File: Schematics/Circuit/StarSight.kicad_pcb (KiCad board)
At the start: 2 copper layers, 21 parts, among them J10 IR1, J11 IR1, J12 ultSound1, J13 ultSound1, J14 ultSound1, J15 ultSound1, J2 Line1, J3 Line2, J4 Line3, J5 Line4, J6 Line5, J7 IR1, J8 IR1, J9 IR1, P1 CONN_13X2, P2 Power, U1 LM1084IT-5.0/NOPB

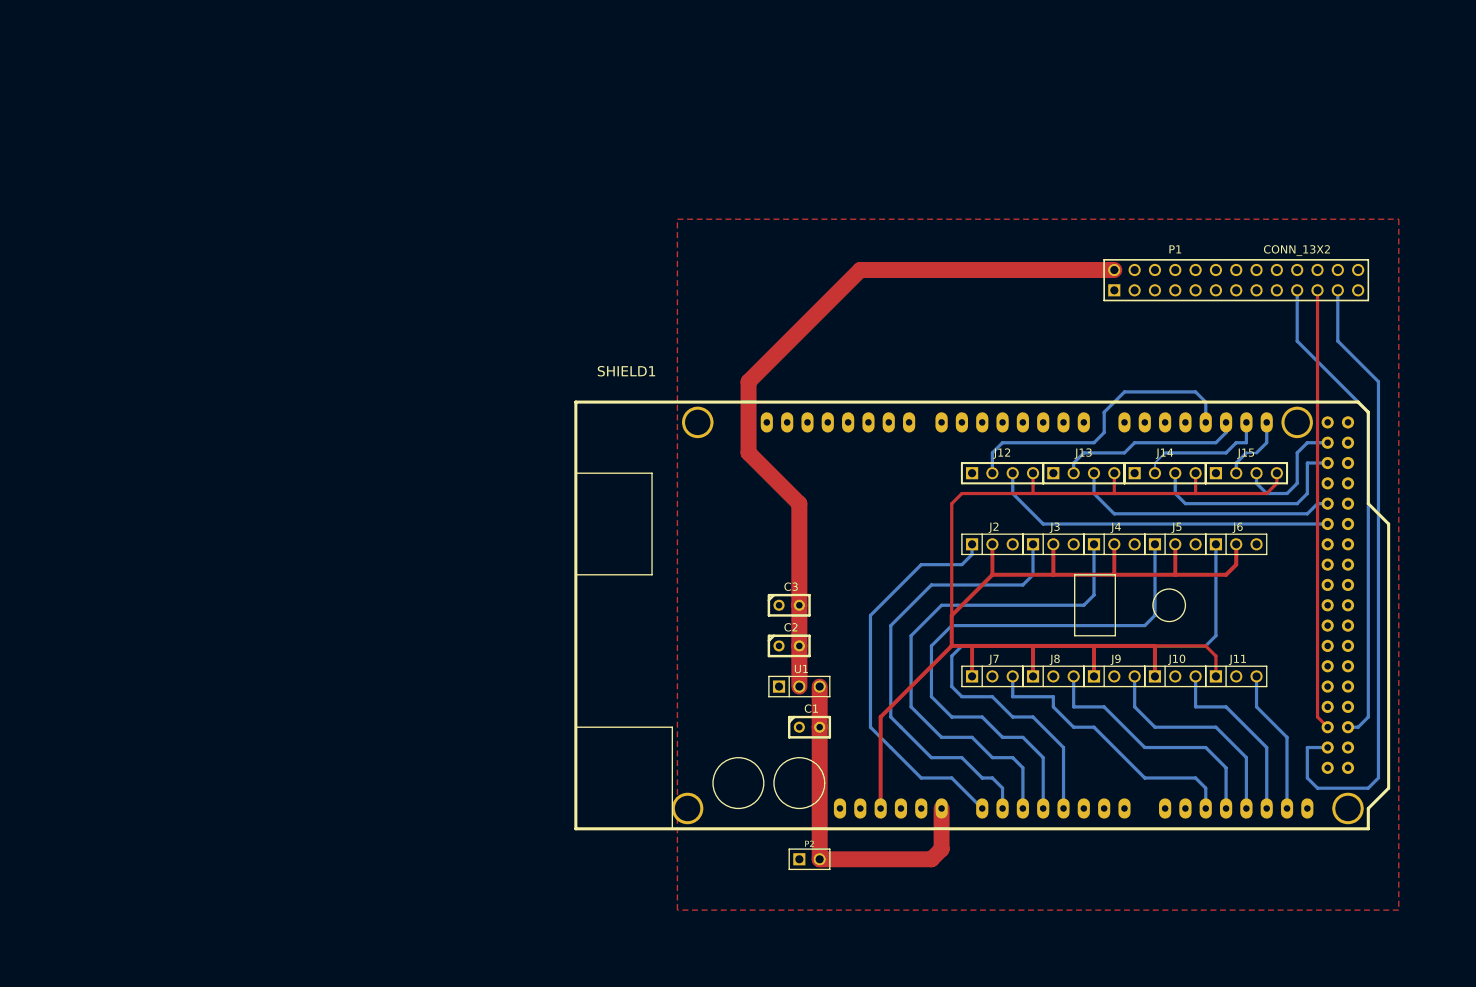
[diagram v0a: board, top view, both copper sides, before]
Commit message: Add switched regulator and motors
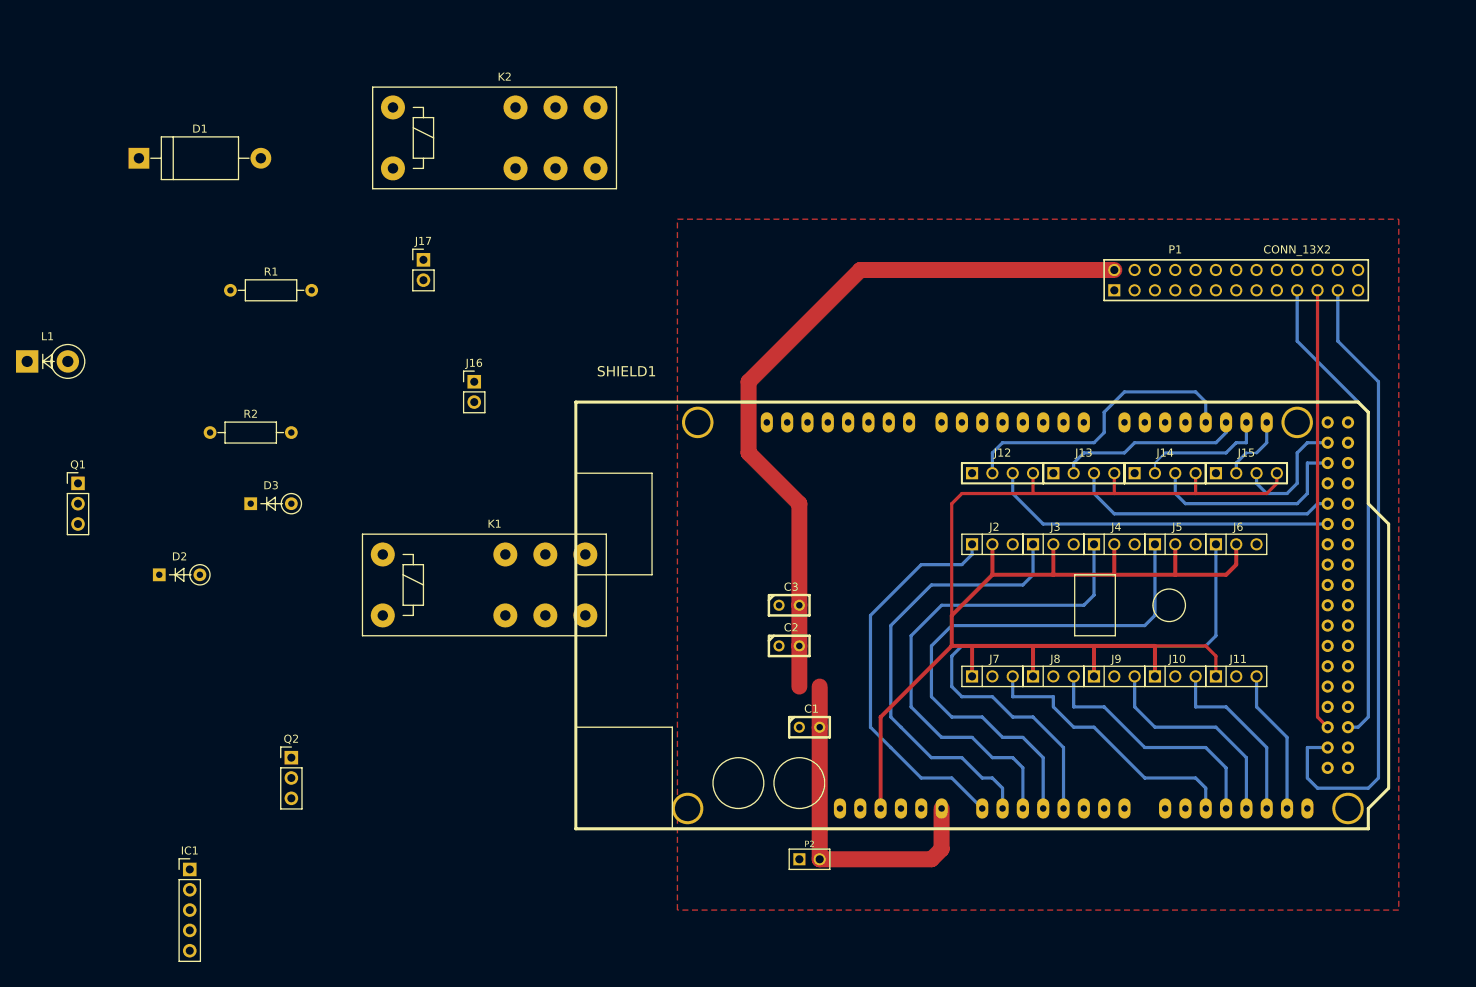
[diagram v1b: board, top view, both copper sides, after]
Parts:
- removed U1: LM1084IT-5.0/NOPB, PIN_ARRAY_3X1
- added D1: 1n5824, Diodes_THT:D_DO-201_P15.24mm_Horizontal, F.Cu at (48.3, 34.3)
- added D2: D, Diodes_THT:D_DO-35_SOD27_P5.08mm_Vertical_KathodeUp, F.Cu at (50.8, 86.4)
- added D3: D, Diodes_THT:D_DO-35_SOD27_P5.08mm_Vertical_KathodeUp, F.Cu at (62.2, 77.5)
- added IC1: LM2956-5V, Pin_Headers:Pin_Header_Straight_1x05_Pitch2.54mm, F.Cu at (54.6, 123.2)
- added J16: Conn_01x02, Pin_Headers:Pin_Header_Straight_1x02_Pitch2.54mm, F.Cu at (90.2, 62.2)
- added J17: Conn_01x02, Pin_Headers:Pin_Header_Straight_1x02_Pitch2.54mm, F.Cu at (83.8, 47.0)
- added K1: M1BS5V2-05T, Relays_THT:Relay_DPDT_Finder_40.52, F.Cu at (78.7, 83.8)
- added K2: M1BS5V2-05T, Relays_THT:Relay_DPDT_Finder_40.52, F.Cu at (80.0, 27.9)
- added L1: 33 uH, Diodes_THT:D_5W_P5.08mm_Vertical_KathodeUp, F.Cu at (34.3, 59.7)
- added Q1: Q_NMOS_GDS, Pin_Headers:Pin_Header_Straight_1x03_Pitch2.54mm, F.Cu at (40.6, 74.9)
- added Q2: Q_NMOS_GDS, Pin_Headers:Pin_Header_Straight_1x03_Pitch2.54mm, F.Cu at (67.3, 109.2)
- added R1: 10k, Resistors_THT:R_Axial_DIN0207_L6.3mm_D2.5mm_P10.16mm_Horizontal, F.Cu at (59.7, 50.8)
- added R2: 10k, Resistors_THT:R_Axial_DIN0207_L6.3mm_D2.5mm_P10.16mm_Horizontal, F.Cu at (57.1, 68.6)
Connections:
- net N-0000085 renamed +12V
- P1 pad 1: (no net) -> Net-(P1-Pad1)
- P1 pad 10: (no net) -> /RXD
- P1 pad 11: (no net) -> /GPIO22
- P1 pad 12: (no net) -> /GPIO18
- P1 pad 13: (no net) -> Net-(P1-Pad13)
- P1 pad 14: (no net) -> Net-(P1-Pad14)
- P1 pad 15: (no net) -> Net-(P1-Pad15)
- P1 pad 16: (no net) -> /GPIO23
- P1 pad 17: (no net) -> Net-(P1-Pad17)
- P1 pad 18: (no net) -> /GPIO24
- P1 pad 20: (no net) -> Net-(P1-Pad20)
- P1 pad 22: (no net) -> /GPIO25
- P1 pad 24: (no net) -> /GPIO8(CE0)
- P1 pad 25: (no net) -> Net-(P1-Pad25)
- P1 pad 26: (no net) -> /GPIO7(CE1)
- P1 pad 3: (no net) -> /GPIO0(SDA)
- P1 pad 4: (no net) -> Net-(P1-Pad4)
- P1 pad 5: (no net) -> /GPIO1(SCL)
- P1 pad 7: (no net) -> /GPIO17
- P1 pad 8: (no net) -> /TXD
- P1 pad 9: (no net) -> Net-(P1-Pad9)
- SHIELD1 pad 0: (no net) -> Net-(SHIELD1-Pad0)
- SHIELD1 pad 1: (no net) -> Net-(SHIELD1-Pad1)
- SHIELD1 pad 10: (no net) -> Net-(Q2-Pad1)
- SHIELD1 pad 11: (no net) -> Net-(K2-PadA2)
- SHIELD1 pad 12: (no net) -> Net-(Q1-Pad1)
- SHIELD1 pad 13: (no net) -> Net-(K1-PadA2)
- SHIELD1 pad 14: (no net) -> Net-(SHIELD1-Pad14)
- SHIELD1 pad 15: (no net) -> Net-(SHIELD1-Pad15)
- SHIELD1 pad 16: (no net) -> Net-(SHIELD1-Pad16)
- SHIELD1 pad 17: (no net) -> Net-(SHIELD1-Pad17)
- SHIELD1 pad 2: (no net) -> Net-(SHIELD1-Pad2)
- SHIELD1 pad 23: (no net) -> Net-(SHIELD1-Pad23)
- SHIELD1 pad 25: (no net) -> Net-(SHIELD1-Pad25)
- SHIELD1 pad 26: (no net) -> Net-(SHIELD1-Pad26)
- SHIELD1 pad 27: (no net) -> Net-(SHIELD1-Pad27)
- SHIELD1 pad 29: (no net) -> Net-(SHIELD1-Pad29)
- SHIELD1 pad 3: (no net) -> Net-(SHIELD1-Pad3)
- SHIELD1 pad 31: (no net) -> Net-(SHIELD1-Pad31)
- SHIELD1 pad 32: (no net) -> Net-(SHIELD1-Pad32)
- SHIELD1 pad 33: (no net) -> Net-(SHIELD1-Pad33)
- SHIELD1 pad 34: (no net) -> Net-(SHIELD1-Pad34)
- SHIELD1 pad 35: (no net) -> Net-(SHIELD1-Pad35)
- SHIELD1 pad 36: (no net) -> Net-(SHIELD1-Pad36)
- SHIELD1 pad 37: (no net) -> Net-(SHIELD1-Pad37)
- SHIELD1 pad 38: (no net) -> Net-(SHIELD1-Pad38)
- SHIELD1 pad 39: (no net) -> Net-(SHIELD1-Pad39)
- SHIELD1 pad 3V3: (no net) -> Net-(SHIELD1-Pad3V3)
- SHIELD1 pad 4: (no net) -> Net-(SHIELD1-Pad4)
- SHIELD1 pad 40: (no net) -> Net-(SHIELD1-Pad40)
- SHIELD1 pad 41: (no net) -> Net-(SHIELD1-Pad41)
- SHIELD1 pad 42: (no net) -> Net-(SHIELD1-Pad42)
- SHIELD1 pad 43: (no net) -> Net-(SHIELD1-Pad43)
- SHIELD1 pad 44: (no net) -> Net-(SHIELD1-Pad44)
- SHIELD1 pad 45: (no net) -> Net-(SHIELD1-Pad45)
- SHIELD1 pad 46: (no net) -> Net-(SHIELD1-Pad46)
- SHIELD1 pad 47: (no net) -> Net-(SHIELD1-Pad47)
- SHIELD1 pad 48: (no net) -> Net-(SHIELD1-Pad48)
- SHIELD1 pad 49: (no net) -> Net-(SHIELD1-Pad49)
- SHIELD1 pad 5: (no net) -> Net-(SHIELD1-Pad5)
- SHIELD1 pad 53: (no net) -> Net-(SHIELD1-Pad53)
- SHIELD1 pad 5V_4: (no net) -> Net-(SHIELD1-Pad5V_4)
- SHIELD1 pad 5V_5: (no net) -> Net-(SHIELD1-Pad5V_5)
- SHIELD1 pad 6: (no net) -> Net-(SHIELD1-Pad6)
- SHIELD1 pad 7: (no net) -> Net-(SHIELD1-Pad7)
- SHIELD1 pad 8: (no net) -> Net-(SHIELD1-Pad8)
- SHIELD1 pad 9: (no net) -> Net-(SHIELD1-Pad9)
- SHIELD1 pad AD15: (no net) -> Net-(SHIELD1-PadAD15)
- SHIELD1 pad AD5: (no net) -> Net-(SHIELD1-PadAD5)
- SHIELD1 pad AD6: (no net) -> Net-(SHIELD1-PadAD6)
- SHIELD1 pad AD7: (no net) -> Net-(SHIELD1-PadAD7)
- SHIELD1 pad AD8: (no net) -> Net-(SHIELD1-PadAD8)
- SHIELD1 pad AD9: (no net) -> Net-(SHIELD1-PadAD9)
- SHIELD1 pad AREF: (no net) -> Net-(SHIELD1-PadAREF)
- SHIELD1 pad GND1: (no net) -> Net-(SHIELD1-PadGND1)
- SHIELD1 pad GND3: (no net) -> Net-(SHIELD1-PadGND3)
- SHIELD1 pad GND4: (no net) -> Net-(SHIELD1-PadGND4)
- SHIELD1 pad GND5: (no net) -> Net-(SHIELD1-PadGND5)
- SHIELD1 pad RST: (no net) -> Net-(SHIELD1-PadRST)

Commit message: Fix pcb power suply and motors
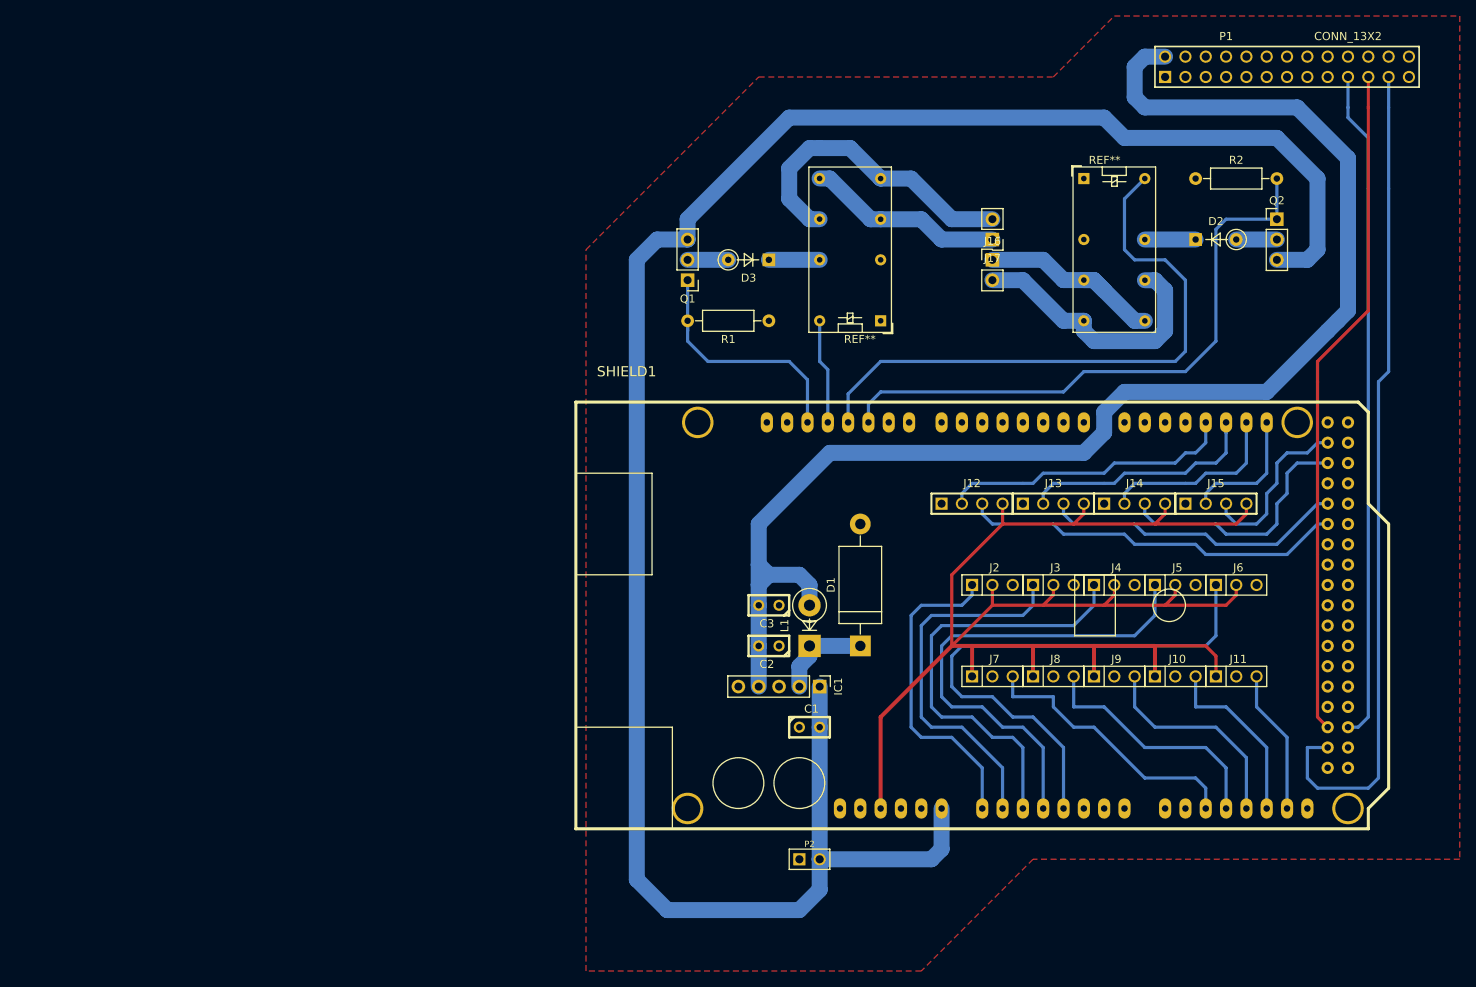
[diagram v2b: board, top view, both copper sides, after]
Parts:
- removed K1, K2: M1BS5V2-05T, Relays_THT:Relay_DPDT_Finder_40.52
- added REF**: Relay_DPDT_Omron_G5V-2, Relays_THT:Relay_DPDT_Omron_G5V-2, F.Cu at (141.0, 54.6)
- added REF**: Relay_DPDT_Omron_G5V-2, Relays_THT:Relay_DPDT_Omron_G5V-2, F.Cu at (166.4, 36.8)
- moved Q2 140.4 mm to (190.5, 41.9)
- moved D2 136.2 mm to (180.3, 44.5)
- moved R2 127.2 mm to (180.3, 36.8)
- moved D1 108.8 mm to (138.4, 95.2), turned to 90 degrees
- moved L1 104.1 mm to (132.1, 95.2), turned to 90 degrees
- moved IC1 82.0 mm to (133.3, 100.3), turned to 270 degrees
- moved Q1 80.3 mm to (116.8, 49.5), turned to 180 degrees
- moved D3 71.6 mm to (127.0, 47.0), turned to 180 degrees
- moved J17 71.2 mm to (154.9, 44.5), turned to 180 degrees
- moved R1 67.4 mm to (127.0, 54.6), turned to 180 degrees
- moved J16 66.5 mm to (154.9, 47.0)
- moved P1 27.4 mm to (191.8, 22.9)
- moved J12 5.39 mm to (152.4, 77.5)
- moved J13 5.39 mm to (162.6, 77.5)
- moved J14 5.39 mm to (172.7, 77.5)
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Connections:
- SHIELD1 pad 12: Net-(Q1-Pad1) -> Net-(K1-PadA2)
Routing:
- net +12V: track 42.4 -> 260.8 mm
- net Net-(C2-Pad2): track 92.2 -> 175.3 mm
- net Net-(Q2-Pad1): track 0.00 -> 76.2 mm
- net Net-(K2-PadA2): track 0.00 -> 76.0 mm
- net Net-(J17-Pad2): track 0.00 -> 38.8 mm
- net Net-(J16-Pad2): track 0.00 -> 34.1 mm
- net Net-(Q1-Pad1): track 0.00 -> 31.2 mm
- net /GPIO9(MISO): track 55.1 -> 84.4 mm
- net Net-(J16-Pad1): track 0.00 -> 25.3 mm
- net /GPIO11(SCLK): track 79.4 -> 104.4 mm
- net Net-(J17-Pad1): track 0.00 -> 24.8 mm
- net /GPIO10(MOSI): track 60.1 -> 84.1 mm
- net +5V: track 199.7 -> 185.3 mm
- net Net-(K1-PadA2): track 0.00 -> 13.1 mm
- net Net-(D1-Pad1): track 0.00 -> 12.0 mm
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
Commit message: Reroute main circuit board to fit 1 dm^2
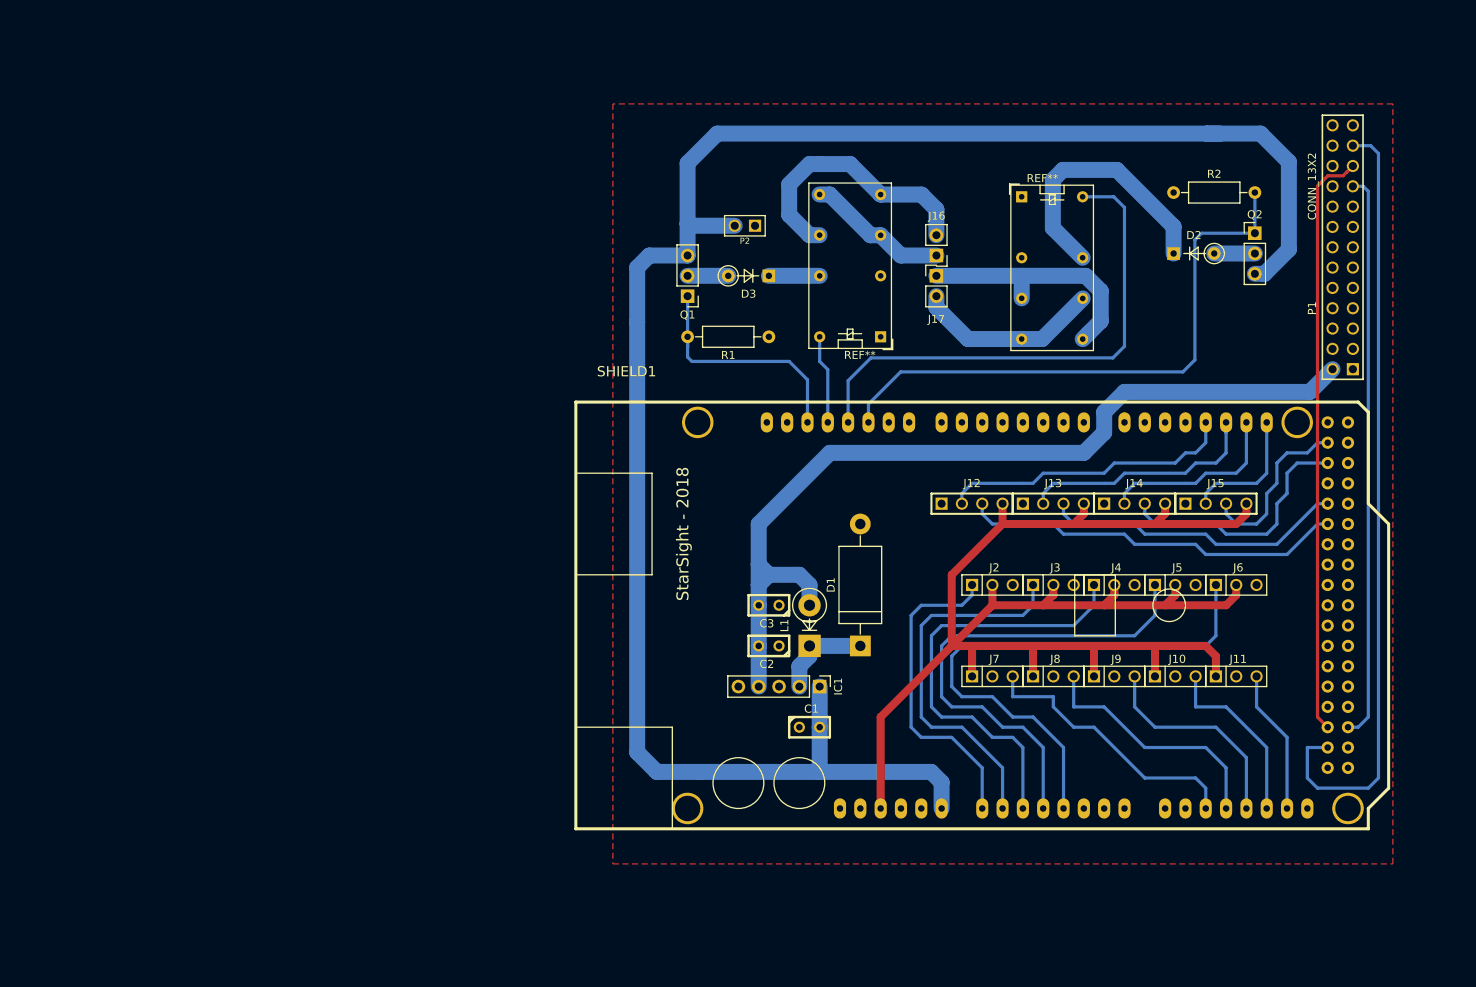
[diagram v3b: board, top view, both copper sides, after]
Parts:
- moved P2 79.6 mm to (124.0, 42.7), turned to 180 degrees
- moved P1 23.6 mm to (198.7, 45.4), turned to 90 degrees
- moved REF** 8.10 mm to (158.6, 39.1)
- moved J16 7.28 mm to (147.9, 49.0)
- moved J17 7.28 mm to (147.9, 46.5)
- moved D2 3.26 mm to (177.6, 46.2)
- moved Q2 3.26 mm to (187.8, 43.7)
- moved R2 3.26 mm to (177.6, 38.6)
- moved D3 2.00 mm to (127.0, 49.0)
- moved Q1 2.00 mm to (116.8, 51.5)
- moved R1 2.00 mm to (127.0, 56.6)
- moved REF** 2.00 mm to (141.0, 56.6)
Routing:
- net Net-(C2-Pad2): track 175.3 -> 113.3 mm
- net Net-(D2-Pad1): track 6.35 -> 33.2 mm
- net +12V: track 260.8 -> 234.9 mm
- net /GPIO10(MOSI): track 84.1 -> 71.0 mm
- net Net-(K2-PadA2): track 76.0 -> 64.7 mm
- net /GPIO9(MISO): track 84.4 -> 73.6 mm
- net Net-(J16-Pad2): track 34.1 -> 23.4 mm
- net Net-(J17-Pad1): track 24.8 -> 17.8 mm
- net /GPIO11(SCLK): track 104.4 -> 98.0 mm
- net Net-(J16-Pad1): track 25.3 -> 31.1 mm
- net Net-(J17-Pad2): track 38.8 -> 33.7 mm
- net Net-(Q2-Pad1): track 76.2 -> 73.3 mm
- net Net-(K1-PadA2): track 13.1 -> 11.1 mm
- net Net-(Q1-Pad1): track 31.2 -> 30.4 mm
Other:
- board text added: "StarSight - 2018"
